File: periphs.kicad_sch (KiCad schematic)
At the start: 1 part, among them U501 STM32L552ZET6Q

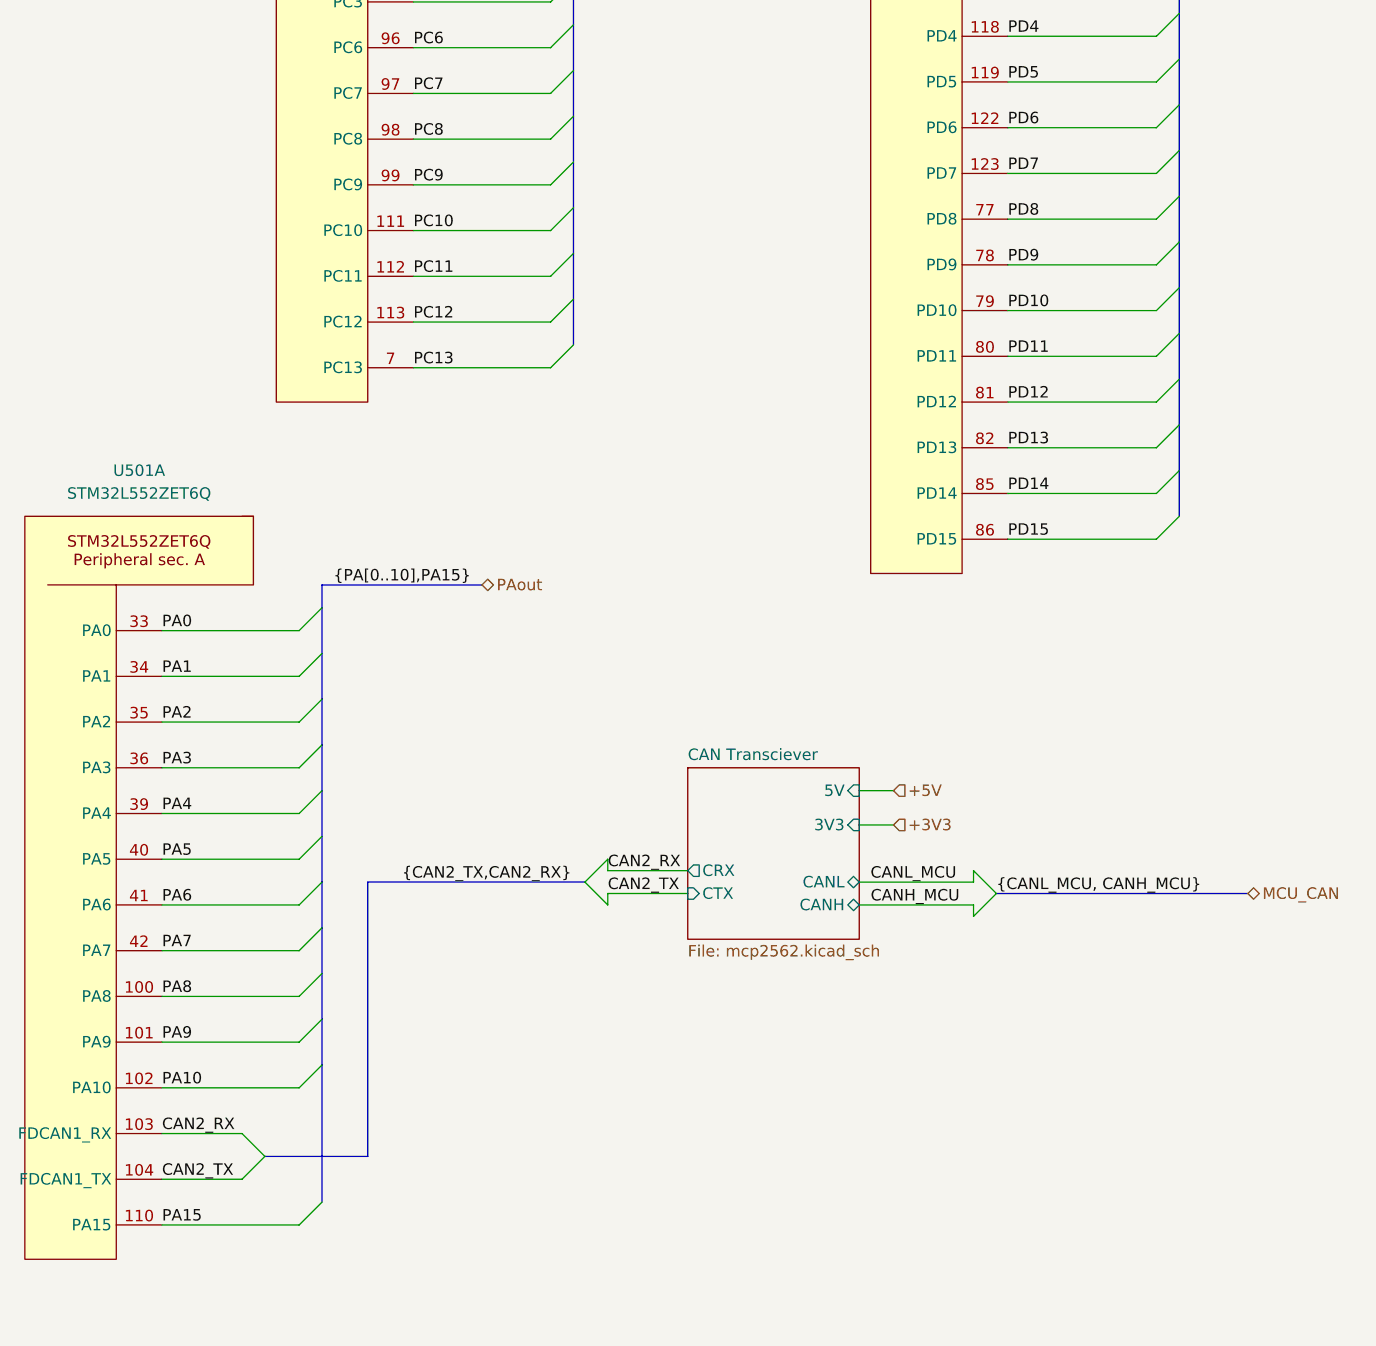
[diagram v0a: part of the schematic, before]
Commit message: jk im stupid forgot to route the flash
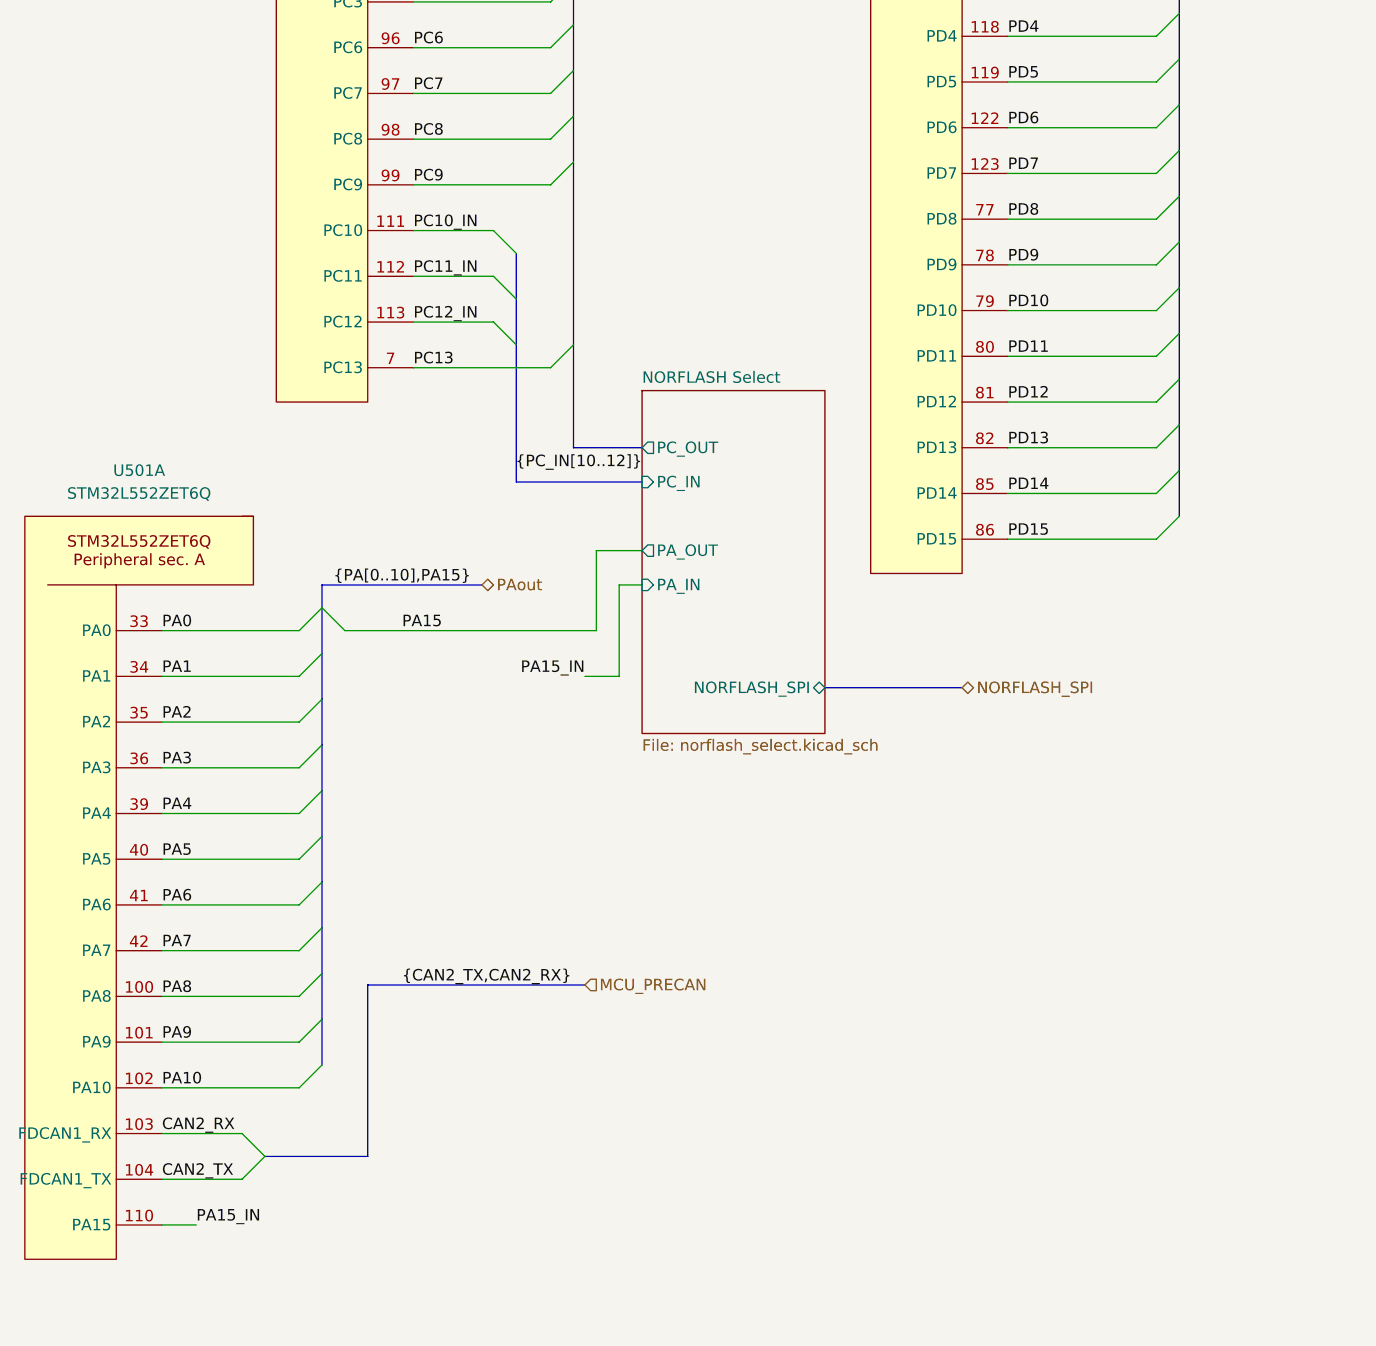
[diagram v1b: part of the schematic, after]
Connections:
- net PA15: no longer U501.110 (PA15)
- net PC10 renamed PC10_IN
- net PC11 renamed PC11_IN
- net PC12 renamed PC12_IN
- new net PA15_IN: U501.110 (PA15)
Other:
- removed sheet CAN Transciever
- added sheet NORFLASH Select (norflash_select.kicad_sch)

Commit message: fixed like a bunch of things, power and new xcvr and lights and other goodies, also started layout
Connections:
- net PF12: no longer U501.47 (PF12)
- net PF13: no longer U501.50 (PF13)
- net PF14: no longer U501.51 (PF14)
- net PF15: no longer U501.52 (PF15)
- new net PF_IN12: U501.47 (PF12)
- new net PF_IN13: U501.50 (PF13)
- new net PF_IN14: U501.51 (PF14)
- new net PF_IN15: U501.52 (PF15)
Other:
- added sheet Debug LED Select (led_arr_sel.kicad_sch)
- moved on the sheet: U501A

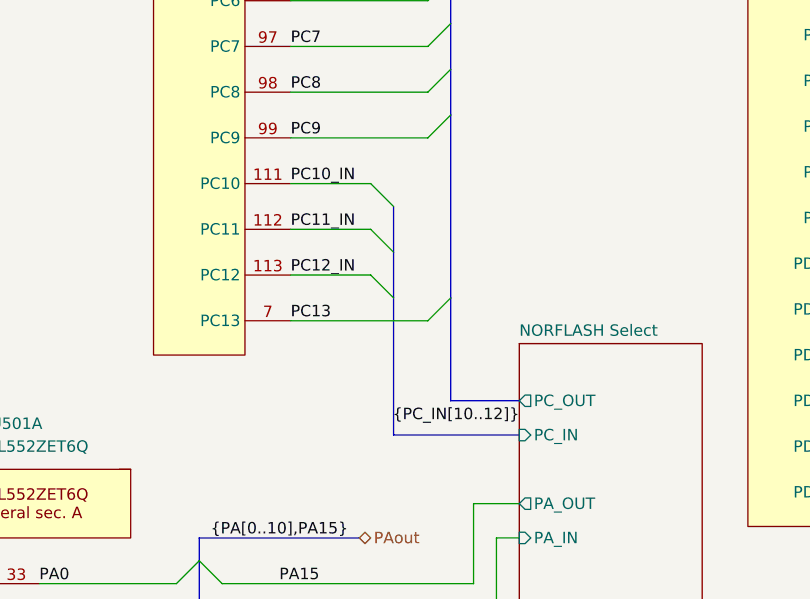
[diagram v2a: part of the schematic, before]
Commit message: quicksave on some R.S. T.S. (mostly layout changes, small pin changes for better routing)
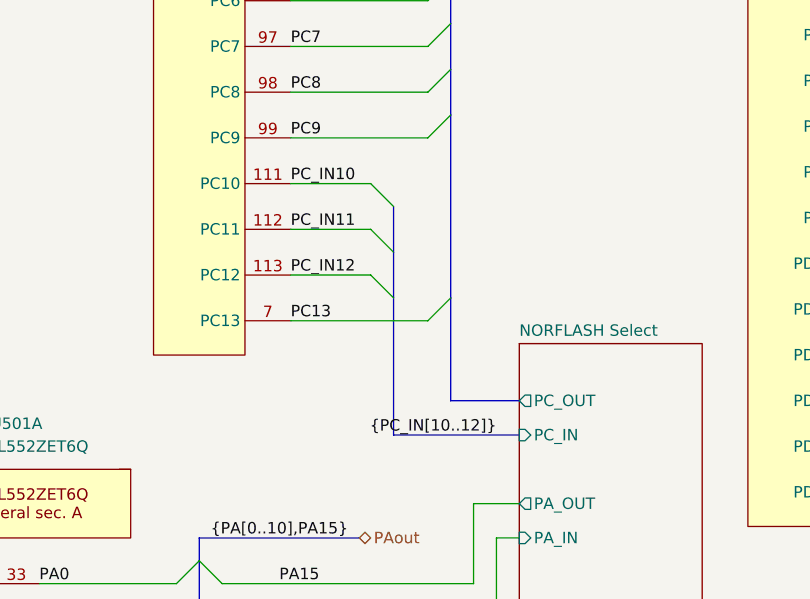
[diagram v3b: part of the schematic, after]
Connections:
- net PC10_IN renamed PC_IN10
- net PC11_IN renamed PC_IN11
- net PC12_IN renamed PC_IN12
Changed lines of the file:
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@@
+		)
+	)
+	(label "PC_IN11"
+		(at 180.34 78.74 0)
+		(effects
+			(font
+				(size 1.27 1.27)
+			)
+			(justify left bottom)
 		)
 	)
@@
 		)
 	)
-	(label "PC12_IN"
-		(at 180.34 83.82 0)
-		(effects
-			(font
-				(size 1.27 1.27)
-			)
-			(justify left bottom)
-		)
-	)
 	(label "PF7"
 		(at 90.17 151.13 0)
@@
 	)
 	(label "{PC_IN[10..12]}"
-		(at 205.74 100.33 180)
+		(at 203.2 101.6 180)
 		(effects
 			(font
@@
 		)
 	)
-	(label "PC11_IN"
-		(at 180.34 78.74 0)
-		(effects
-			(font
-				(size 1.27 1.27)
-			)
-			(justify left bottom)
-		)
-	)
-	(label "PC10_IN"
-		(at 180.34 73.66 0)
-		(effects
-			(font
-				(size 1.27 1.27)
-			)
-			(justify left bottom)
-		)
-	)
 	(label "PG0"
 		(at 29.21 31.75 0)
@@
 		)
 	)
+	(label "PC_IN10"
+		(at 180.34 73.66 0)
+		(effects
+			(font
+				(size 1.27 1.27)
+			)
+			(justify left bottom)
+		)
+	)
 	(label "PB10"
 		(at 107.95 72.39 0)
@@
 		(effects
 			(font
+				(size 1.27 1.27)
+			)
+			(justify left bottom)
+		)
+	)
+	(label "PC_IN12"
+		(at 180.34 83.82 0)
+		(effects
+			(font

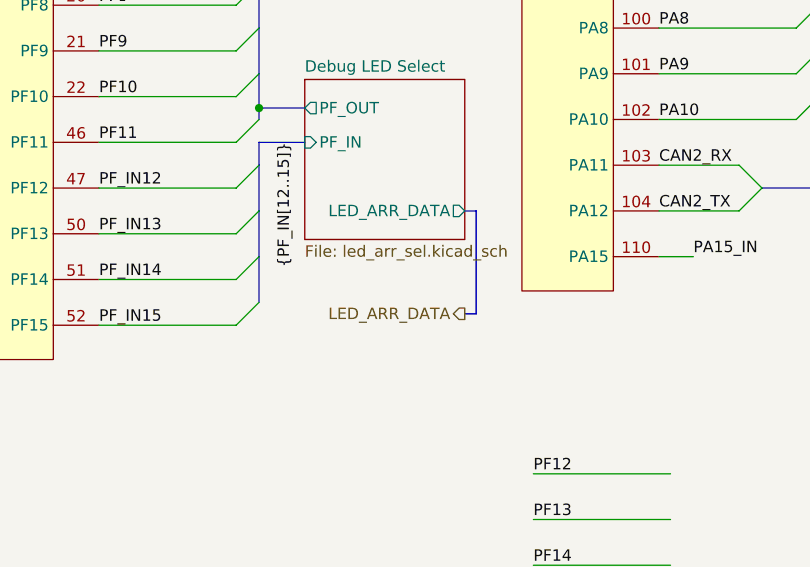
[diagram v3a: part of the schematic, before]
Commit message: laid out most of power, main xcvr, prob some other stuff
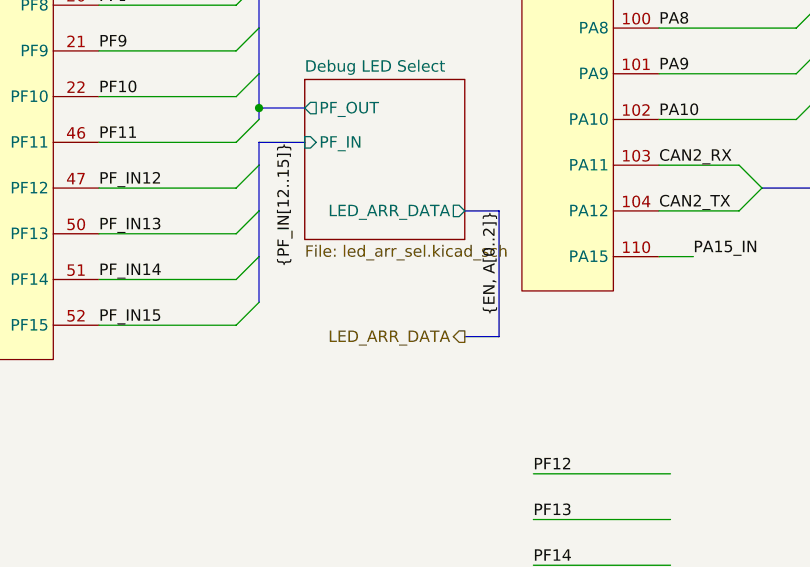
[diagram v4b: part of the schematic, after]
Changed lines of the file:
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@@
 	(bus
 		(pts
-			(xy 130.81 179.07) (xy 132.08 179.07)
+			(xy 130.81 179.07) (xy 134.62 179.07)
 		)
 		(stroke
@@
 	(bus
 		(pts
-			(xy 132.08 179.07) (xy 132.08 190.5)
+			(xy 134.62 179.07) (xy 134.62 193.04)
 		)
 		(stroke
@@
 	(bus
 		(pts
-			(xy 130.81 190.5) (xy 132.08 190.5)
+			(xy 130.81 193.04) (xy 134.62 193.04)
 		)
 		(stroke
@@
 	(label "PA15_IN"
 		(at 199.39 123.19 180)
+		(effects
+			(font
+				(size 1.27 1.27)
+			)
+			(justify right bottom)
+		)
+	)
+	(label "{EN, A[0..2]}"
+		(at 134.62 179.07 270)
 		(effects
 			(font
@@
 	(hierarchical_label "LED_ARR_DATA"
 		(shape output)
-		(at 130.81 190.5 180)
-		(effects
-			(font
+		(at 130.81 193.04 180)
+		(effects
+			(font
